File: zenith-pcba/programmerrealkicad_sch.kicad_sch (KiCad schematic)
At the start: 3 parts, among them J1 USB_C_Receptacle_USB2.0_16P, U1 XC7A50T-CSG325, U3 CH347T

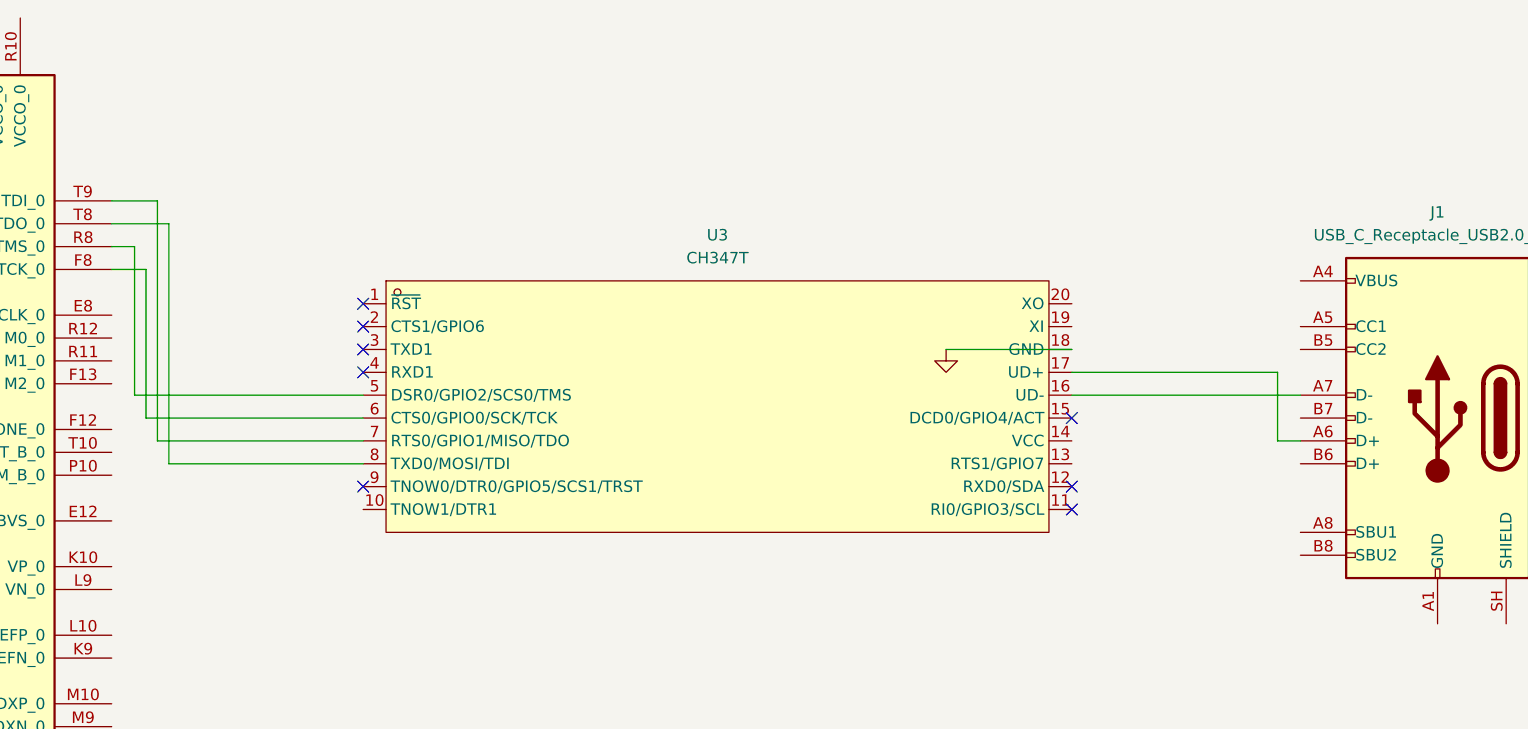
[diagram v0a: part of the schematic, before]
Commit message: feat(pcba): programmer connections and uart
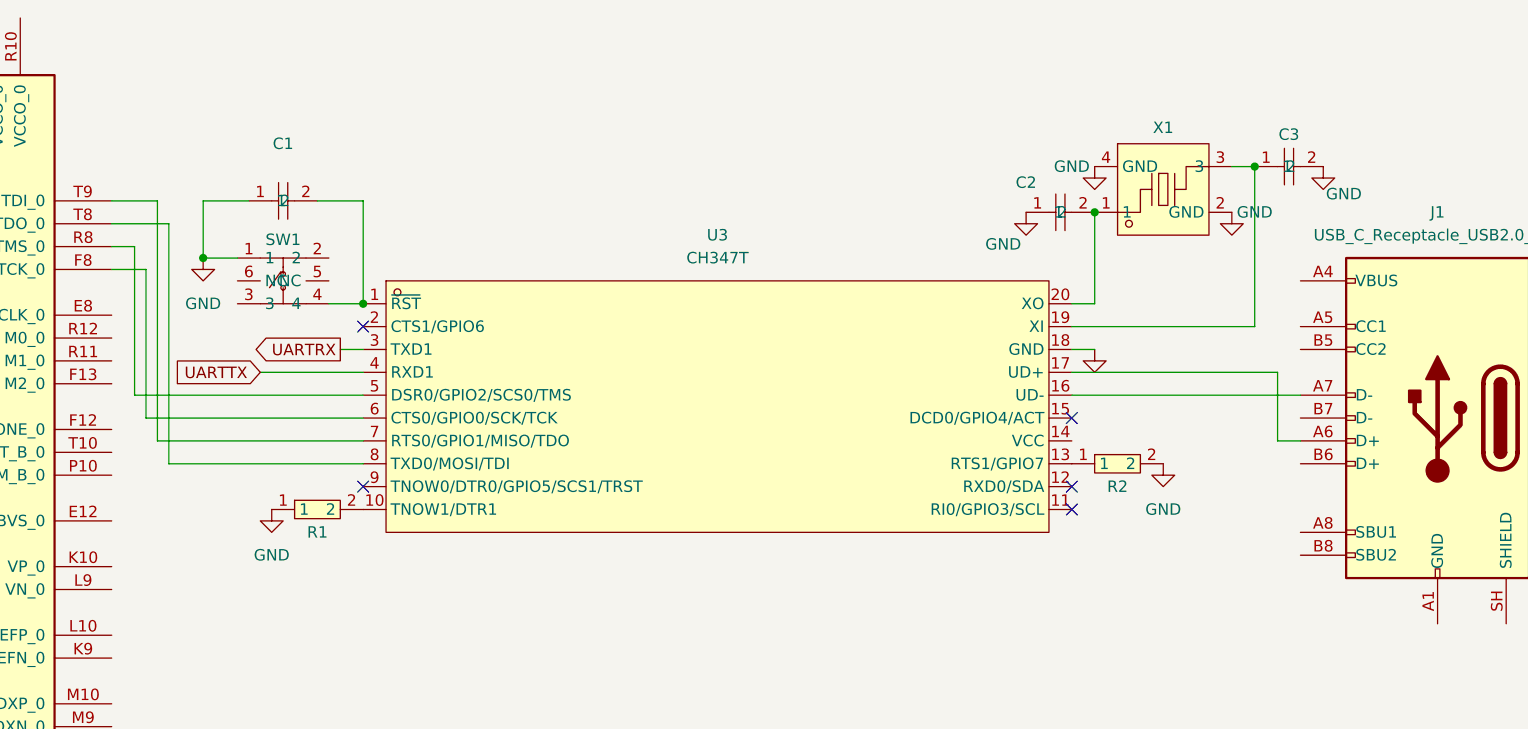
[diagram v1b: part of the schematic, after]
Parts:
- added C1: CL10B104KA8NNNC, easyeda2kicad:C0603, symbol easyeda2kicad:CL10B104KA8NNNC
- added C2, C3: 0402CG220J500NT, easyeda2kicad:C0402, symbol easyeda2kicad:0402CG220J500NT
- added R1, R2: RC0603FR-074K7L, easyeda2kicad:R0603, symbol easyeda2kicad:RC0603FR-074K7L
- added SW1: G4R152312, easyeda2kicad:SW-SMD_4P-L5.2-W5.2-P3.70-LS6.4_UK-B0233XX, symbol easyeda2kicad:G4R152312
- added X1: SX5B8.000F1520F30, easyeda2kicad:CYSTAL-SMD_4P-L5.0-W3.2-BL, symbol easyeda2kicad:SX5B8.000F1520F30
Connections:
- net GND: now also C1.1, C2.1, C3.2, R1.1, R2.2, SW1.1, X1.2 (GND), X1.4 (GND)
- net at U3.1 (~{RST}): now also C1.2, SW1.4
- net at U3.10 (TNOW1/DTR1): now also R1.2
- net at U3.13 (RTS1/GPIO7): now also R2.1
- net at U3.19 (XI): now also C3.1, X1.3
- net at U3.20 (XO): now also C2.2, X1.1
- net UARTRX: now reaches U3.3 (TXD1)
- net UARTTX: now reaches U3.4 (RXD1)
- no-connect marks 8 -> 5

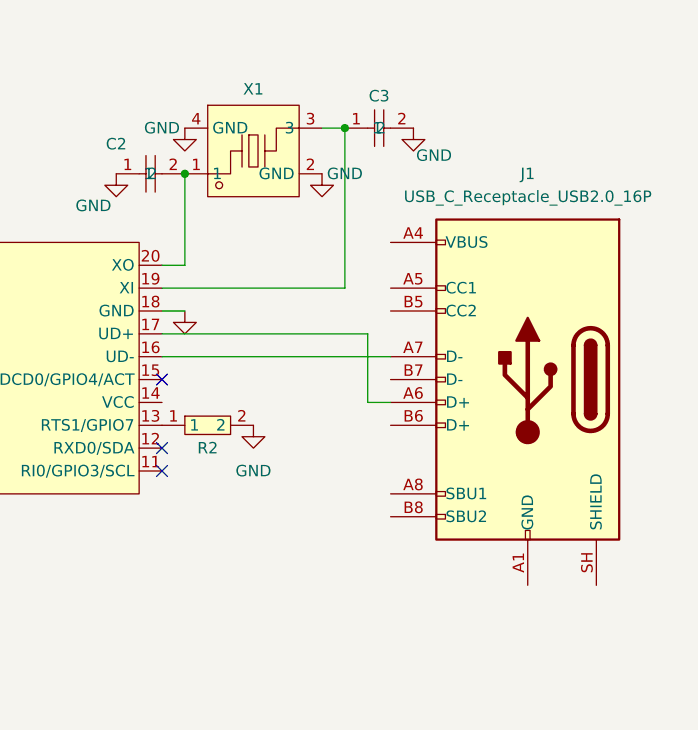
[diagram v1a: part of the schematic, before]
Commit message: fix(pcba): 3d models
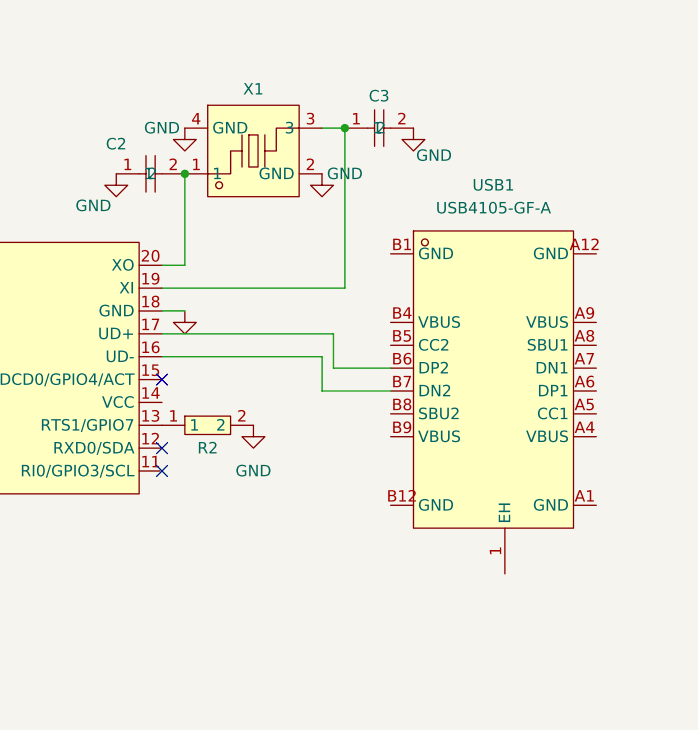
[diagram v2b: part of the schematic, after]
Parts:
- removed J1: USB_C_Receptacle_USB2.0_16P, Connector_USB:USB_C_Receptacle_GCT_USB4105-xx-A_16P_TopMnt_Horizontal, symbol Connector:USB_C_Receptacle_USB2.0_16P
- added USB1: USB4105-GF-A, easyeda2kicad:TYPE-C-SMD_SBC-160S1A-20-S412, symbol easyeda2kicad:USB4105-GF-A
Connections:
- net at U3.17 (UD+): now also USB1.B6 (DP2)
- net at U3.16 (UD-): now also USB1.B7 (DN2)
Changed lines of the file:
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@@
+	(wire
+		(pts
+			(xy 229.87 69.85) (xy 223.52 69.85)
+		)
+		(stroke
+			(width 0)
+			(type default)
+		)
+	)
 	(wire
 		(pts
@@
 	(wire
 		(pts
+			(xy 223.52 66.04) (xy 204.47 66.04)
+		)
+		(stroke
+			(width 0)
+			(type default)
+		)
+	)
+	(wire
+		(pts
 			(xy 102.87 73.66) (xy 102.87 46.99)
 		)
@@
 	(wire
 		(pts
-			(xy 204.47 68.58) (xy 229.87 68.58)
-		)
-		(stroke
-			(width 0)
-			(type default)
-		)
-	)
-	(wire
-		(pts
 			(xy 120.65 46.99) (xy 125.73 46.99)
 		)
@@
 	(wire
 		(pts
+			(xy 222.25 72.39) (xy 229.87 72.39)
+		)
+		(stroke
+			(width 0)
+			(type default)
+		)
+	)
+	(wire
+		(pts
+			(xy 223.52 69.85) (xy 223.52 66.04)
+		)
+		(stroke
+			(width 0)
+			(type default)
+		)
+	)
+	(wire
+		(pts
 			(xy 123.19 63.5) (xy 125.73 63.5)
 		)
@@
 	(wire
 		(pts
-			(xy 204.47 66.04) (xy 227.33 66.04)
-		)
-		(stroke
-			(width 0)
-			(type default)
-		)
-	)
-	(wire
-		(pts
 			(xy 107.95 46.99) (xy 107.95 53.34)
 		)
@@
 	(wire
 		(pts
-			(xy 227.33 73.66) (xy 229.87 73.66)
-		)
-		(stroke
-			(width 0)
-			(type default)
-		)
-	)
-	(wire
-		(pts
-			(xy 227.33 66.04) (xy 227.33 73.66)
-		)
-		(stroke
-			(width 0)
-			(type default)
-		)
-	)
-	(wire
-		(pts
 			(xy 114.3 66.04) (xy 125.73 66.04)
 		)
@@
 	(wire
 		(pts
+			(xy 222.25 68.58) (xy 222.25 72.39)
+		)
+		(stroke
+			(width 0)
+			(type default)
+		)
+	)
+	(wire
+		(pts
 			(xy 204.47 58.42) (xy 207.01 58.42)
 		)
@@
 		(pts
 			(xy 125.73 73.66) (xy 102.87 73.66)
+		)
+		(stroke
+			(width 0)
+			(type default)
+		)
+	)
+	(wire
+		(pts
+			(xy 204.47 68.58) (xy 222.25 68.58)
 		)
 		(stroke
@@
 				(path "/998c5703-2ef0-4484-8ced-1d53dcc65d39/d152660c-456e-437b-9b9b-57a28d7a418e"
 					(reference "R2")
-					(unit 1)
-				)
-			)
-		)
-	)
-	(symbol
-		(lib_id "Connector:USB_C_Receptacle_USB2.0_16P")
-		(at 245.11 71.12 0)
-		(mirror y)
-		(unit 1)
-		(body_style 1)
-		(exclude_from_sim no)
-		(in_bom yes)
-		(on_board yes)
-		(in_pos_files yes)
-		(dnp no)
-		(property "Reference" "J1"
-			(at 245.11 48.26 0)
-			(show_name no)
-			(do_not_autoplace no)
-			(effects
-				(font
-					(size 1.27 1.27)
-				)
-			)
-		)
-		(property "Value" "USB_C_Receptacle_USB2.0_16P"
-			(at 245.11 50.8 0)
-			(show_name no)
-			(do_not_autoplace no)
-			(effects
-				(font
-					(size 1.27 1.27)
-				)
-			)
-		)
-		(property "Footprint" "Connector_USB:USB_C_Receptacle_GCT_USB4105-xx-A_16P_TopMnt_Horizontal"
-			(at 241.3 71.12 0)
-			(hide yes)
-			(show_name no)
-			(do_not_autoplace no)
-			(effects
-				(font
-					(size 1.27 1.27)
-				)
-			)
-		)
-		(property "Datasheet" "https://www.usb.org/sites/default/files/documents/usb_type-c.zip"
-			(at 241.3 71.12 0)
-			(hide yes)
-			(show_name no)
-			(do_not_autoplace no)
-			(effects
-				(font
-					(size 1.27 1.27)
-				)
-			)
-		)
-		(property "Description" "USB 2.0-only 16P Type-C Receptacle connector"
-			(at 245.11 71.12 0)
-			(hide yes)
-			(show_name no)
-			(do_not_autoplace no)
-			(effects
-				(font
-					(size 1.27 1.27)
-				)
-			)
-		)
-		(pin "B1"
-		)
-		(pin "B4"
-		)
-		(pin "B8"
-		)
-		(pin "B6"
-		)
-		(pin "B7"
-		)
-		(pin "B5"
-		)
-		(pin "SH"
-		)
-		(pin "A12"
-		)
-		(pin "B9"
-		)
-		(pin "A5"
-		)
-		(pin "A7"
-		)
-		(pin "A1"
-		)
-		(pin "B12"
-		)
-		(pin "A9"
-		)
-		(pin "A8"
-		)
-		(pin "A6"
-		)
-		(pin "A4"
-		)
-		(instances
-			(project "zenith-pcba"
-				(path "/998c5703-2ef0-4484-8ced-1d53dcc65d39/d152660c-456e-437b-9b9b-57a28d7a418e"
-					(reference "J1")
 					(unit 1)
 				)
@@
 					(unit 1)
 				)
+			)
+		)
+	)
+	(symbol
+		(lib_id "easyeda2kicad:USB4105-GF-A")
+		(at 241.3 73.66 0)
+		(unit 1)
+		(body_style 1)
+		(exclude_from_sim no)
+		(in_bom yes)
+		(on_board yes)
+		(in_pos_files yes)
+		(dnp no)
+		(fields_autoplaced yes)
+		(property "Reference" "USB1"
+			(at 241.3 49.53 0)
+			(show_name no)
+			(do_not_autoplace no)
+			(effects
+				(font
+					(size 1.27 1.27)
+				)
+			)
+		)
+		(property "Value" "USB4105-GF-A"
+			(at 241.3 52.07 0)
+			(show_name no)
+			(do_not_autoplace no)
+			(effects
+				(font
+					(size 1.27 1.27)
+				)
+			)
+		)
+		(property "Footprint" "easyeda2kicad:TYPE-C-SMD_SBC-160S1A-20-S412"
+			(at 241.3 100.33 0)
+			(hide yes)
+			(show_name no)
+			(do_not_autoplace no)
+			(effects
+				(font
+					(size 1.27 1.27)
+				)
+			)
+		)
+		(property "Datasheet" "https://www.lcsc.com/datasheet/C3020560.pdf"
+			(at 241.3 102.87 0)
+			(hide yes)
+			(show_name no)
+			(do_not_autoplace no)
+			(effects
+				(font
+					(size 1.27 1.27)
+				)
+			)
+		)
+		(property "Description" ""
+			(at 241.3 73.66 0)
+			(hide yes)
+			(show_name no)
+			(do_not_autoplace no)
+			(effects
+				(font
+					(size 1.27 1.27)
+				)
+			)
+		)
+		(property "Manufacturer" "GCT"
+			(at 241.3 105.41 0)
+			(hide yes)
+			(show_name no)
+			(do_not_autoplace no)
+			(effects
+				(font
+					(size 1.27 1.27)
+				)
+			)
+		)
+		(property "MPN" "USB4105-GF-A"
+			(at 241.3 107.95 0)
+			(hide yes)
+			(show_name no)
+			(do_not_autoplace no)
+			(effects
+				(font
+					(size 1.27 1.27)
+				)
+			)
+		)
+		(property "LCSC Part" "C3020560"
+			(at 241.3 110.49 0)
+			(hide yes)
+			(show_name no)
+			(do_not_autoplace no)
+			(effects
+				(font
+					(size 1.27 1.27)
+				)
+			)
+		)
+		(pin "A4"
+		)
+		(pin "A1"
+		)
+		(pin "B6"
+		)
+		(pin "B9"
+		)
+		(pin "B7"
+		)
+		(pin "B1"
+		)
+		(pin "1"
+		)
+		(pin "A7"
+		)
+		(pin "A8"
+		)
+		(pin "A9"
+		)
+		(pin "B12"
+		)
+		(pin "A5"
+		)
+		(pin "B8"
+		)
+		(pin "B5"
+		)
+		(pin "A6"
+		)
+		(pin "B4"
+		)
+		(pin "A12"
+		)
+		(instances
+			(project "zenith-pcba"
+				(path "/998c5703-2ef0-4484-8ced-1d53dcc65d39/d152660c-456e-437b-9b9b-57a28d7a418e"
+					(reference "USB1")
+					(unit 1)
+				)

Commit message: fix(pcba): data routing
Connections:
- net GND: now also SW1.5 (NC), SW1.6 (NC), USB1.A1 (GND), USB1.A12 (GND), USB1.B1 (GND), USB1.B12 (GND)
- net at U3.16 (UD-), USB1.B7 (DN2): now also USB1.A7 (DN1)
- net at U3.17 (UD+), USB1.B6 (DP2): now also USB1.A6 (DP1)
- no-connect marks 5 -> 7

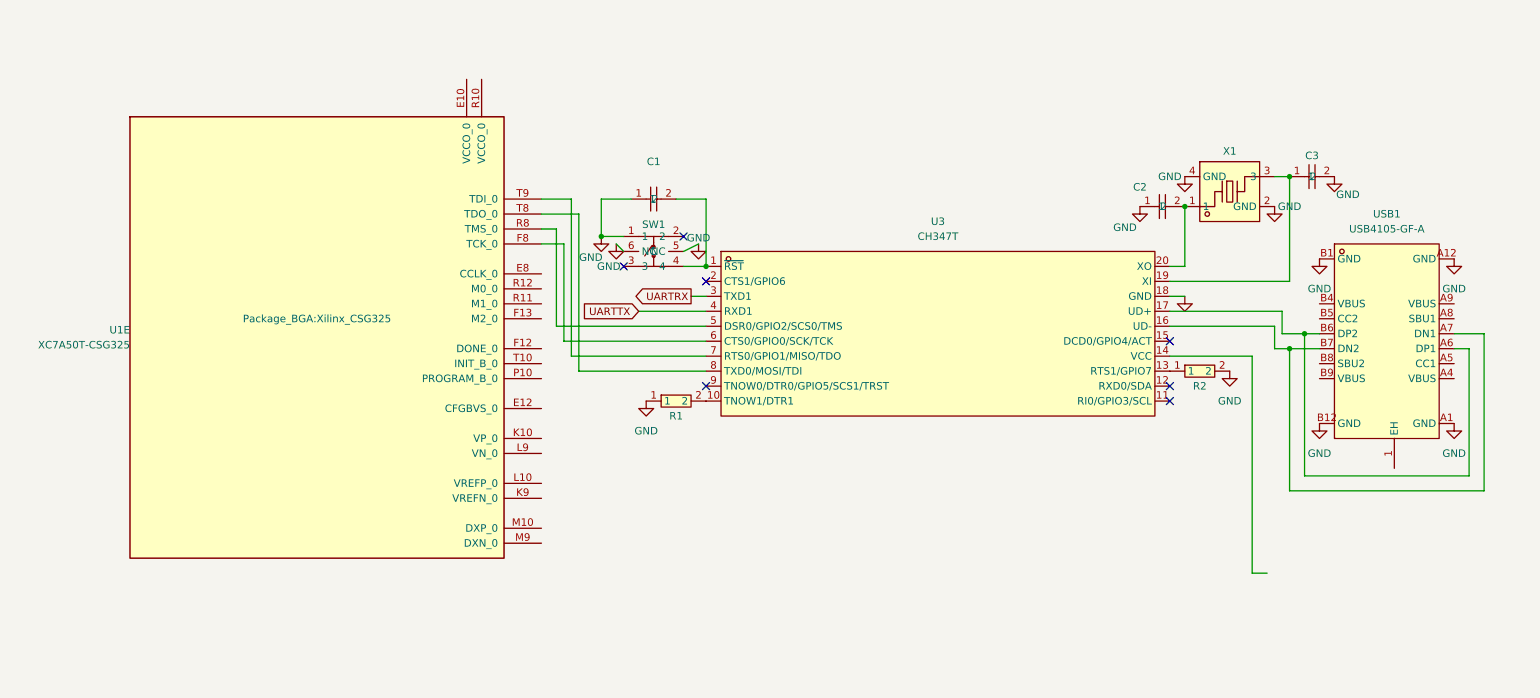
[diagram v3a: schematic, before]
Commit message: feat(pcba): usb esd
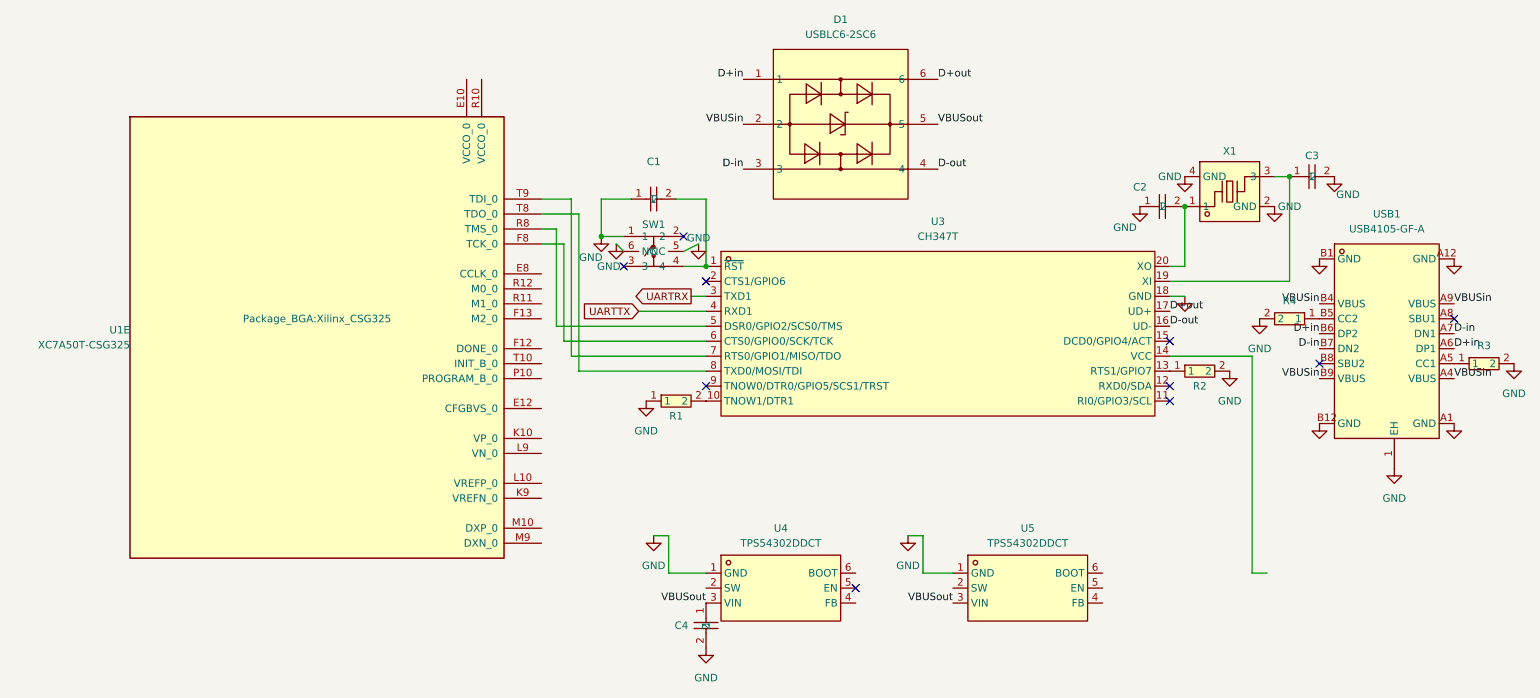
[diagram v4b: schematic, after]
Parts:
- added C4: CC0603MRX5R7BB106, easyeda2kicad:C0603, symbol easyeda2kicad:CC0603MRX5R7BB106
- added D1: USBLC6-2SC6, easyeda2kicad:SOT-23-6_L2.9-W1.6-P0.95-LS2.8-BL, symbol easyeda2kicad:USBLC6-2SC6
- added R3, R4: RC0603JR-075K1L, easyeda2kicad:R0603, symbol easyeda2kicad:RC0603JR-075K1L
- added U4, U5: TPS54302DDCT, easyeda2kicad:TSOT-23-6_L2.9-W1.6-P0.95-LS2.8-BR, symbol easyeda2kicad:TPS54302DDCT
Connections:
- net GND: now also USB1.1 (EH), C4.2, R3.2, R4.2, U4.1 (GND), U5.1 (GND)
- net D-in: now reaches USB1.A7 (DN1), USB1.B7 (DN2)
- net D-in: now also D1.3; no longer U3.16 (UD-)
- net D+in: now reaches USB1.A6 (DP1), USB1.B6 (DP2)
- net D+in: now also D1.1; no longer U3.17 (UD+)
- net VBUSin: now reaches USB1.A4 (VBUS)
- net VBUSin: now also USB1.A9 (VBUS), USB1.B4 (VBUS), USB1.B9 (VBUS), D1.2
- net at USB1.A5 (CC1): now also R3.1
- net at USB1.B5 (CC2): now also R4.1
- new net D+out: D1.6, U3.17 (UD+)
- new net D-out: D1.4, U3.16 (UD-)
- new net VBUSout: C4.1, D1.5, U4.3 (VIN), U5.3 (VIN)
- no-connect marks 7 -> 10

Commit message: fix(pcba): usb c esd ground
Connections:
- net VBUSout is gone; now on net VBUSin: C4.1, D1.5, U4.3 (VIN), U5.3 (VIN)
- net GND: now also D1.2
- net VBUSin: no longer D1.2
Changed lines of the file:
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@@
 		)
 	)
-	(label "VBUSout"
+	(label "VBUSin"
 		(at 165.1 34.29 0)
 		(effects
@@
 		)
 	)
-	(label "VBUSout"
+	(label "VBUSin"
 		(at 167.64 115.57 180)
 		(effects
@@
 		)
 	)
-	(label "VBUSin"
-		(at 132.08 34.29 180)
-		(effects
-			(font
-				(size 1.27 1.27)
-			)
-			(justify right bottom)
-		)
-	)
 	(label "D-in"
 		(at 132.08 41.91 180)
@@
 		)
 	)
-	(label "VBUSout"
+	(label "VBUSin"
 		(at 125.73 115.57 180)
 		(effects
@@
 					(unit 1)
 				)
+			)
+		)
+	)
+	(symbol
+		(lib_id "power:GND")
+		(at 132.08 34.29 0)
+		(unit 1)
+		(body_style 1)
+		(exclude_from_sim no)
+		(in_bom yes)
+		(on_board yes)
+		(in_pos_files yes)
+		(dnp no)
+		(property "Reference" "#PWR021"
+			(at 132.08 40.64 0)
+			(hide yes)
+			(show_name no)
+			(do_not_autoplace no)
+			(effects
+				(font
+					(size 1.27 1.27)
+				)
+			)
+		)
+		(property "Value" "GND"
+			(at 128.778 34.29 0)
+			(show_name no)
+			(do_not_autoplace no)
+			(effects
+				(font
+					(size 1.27 1.27)
+				)
+			)
+		)
+		(property "Footprint" ""
+			(at 132.08 34.29 0)
+			(hide yes)
+			(show_name no)
+			(do_not_autoplace no)
+			(effects
+				(font
+					(size 1.27 1.27)
+				)
+			)
+		)
+		(property "Datasheet" ""
+			(at 132.08 34.29 0)
+			(hide yes)
+			(show_name no)
+			(do_not_autoplace no)
+			(effects
+				(font
+					(size 1.27 1.27)
+				)
+			)
+		)
+		(property "Description" "Power symbol creates a global label with name \"GND\" , ground"
+			(at 132.08 34.29 0)
+			(hide yes)
+			(show_name no)
+			(do_not_autoplace no)
+			(effects
+				(font
+					(size 1.27 1.27)
+				)
+			)
+		)
+		(pin "1"
+		)
+		(instances
+			(project "zenith-pcba"
+				(path "/998c5703-2ef0-4484-8ced-1d53dcc65d39/d152660c-456e-437b-9b9b-57a28d7a418e"
+					(reference "#PWR021")
+					(unit 1)
+				)
